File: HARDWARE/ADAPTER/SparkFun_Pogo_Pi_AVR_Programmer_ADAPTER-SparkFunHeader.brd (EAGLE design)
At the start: 15.2 x 31.8 mm, 15 parts, among them J2 CABLE

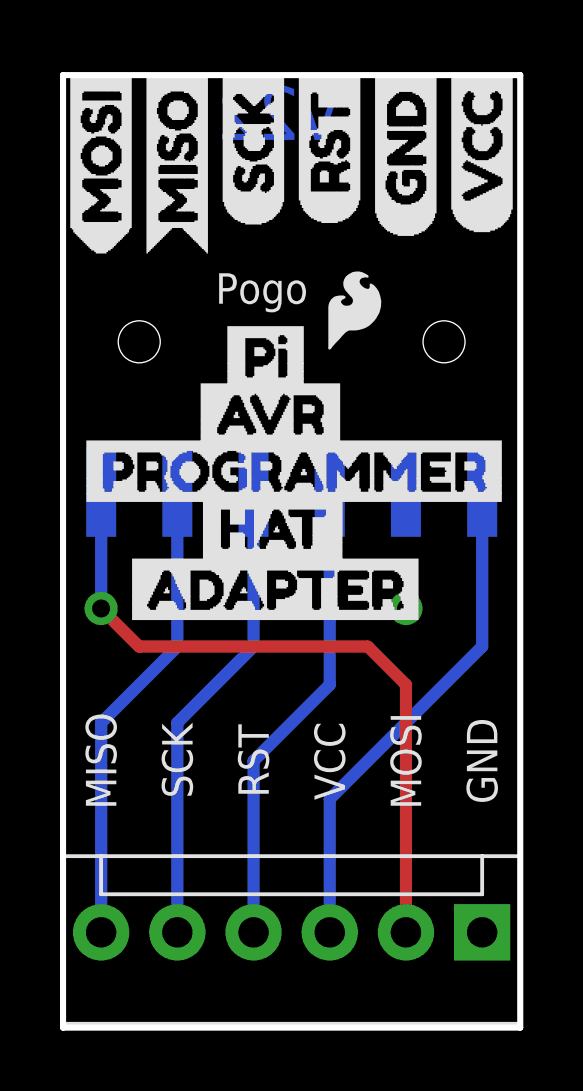
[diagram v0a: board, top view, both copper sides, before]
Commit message: Added proper pogo header.
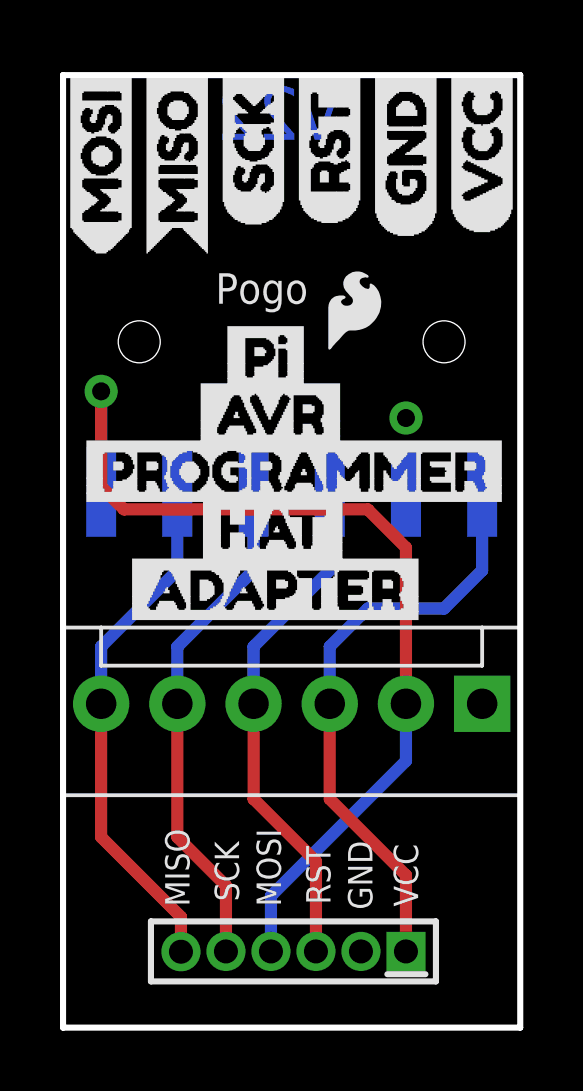
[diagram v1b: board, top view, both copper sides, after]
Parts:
- added U$12: AVR_MINI_PROGSMD, SparkFun-Connectors:AVR_MINI_PROG
- moved JP1 7.62 mm to (14.0, 10.8)
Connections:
- net GND_C: now also U$12.2
- net MISO_C: now also U$12.6
- net MOSI_C: now also U$12.4
- net RST_C: now also U$12.3
- net SCK_C: now also U$12.5
- net VCC_C: now also U$12.1
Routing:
- net MOSI_C: track 23.4 -> 32.9 mm
- net VCC_C: track 16.8 -> 20.0 mm
- net MISO_C: track 15.7 -> 17.5 mm
- net RST_C: track 15.7 -> 17.2 mm
- net SCK_C: track 15.7 -> 17.0 mm
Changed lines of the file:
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@@
 <text x="-10.16" y="-15.24" size="1.778" layer="19" font="vector">Modified by: Michael Moskie</text>
 <text x="5.08" y="24.13" size="1.016" layer="21" font="vector">Pogo</text>
-<text x="1.27" y="8.89" size="1.016" layer="21" font="vector" rot="R90" align="center">MISO</text>
-<text x="3.81" y="8.89" size="1.016" layer="21" font="vector" rot="R90" align="center">SCK</text>
-<text x="6.35" y="8.89" size="1.016" layer="21" font="vector" rot="R90" align="center">RST</text>
-<text x="8.89" y="8.89" size="1.016" layer="21" font="vector" rot="R90" align="center">VCC</text>
-<text x="11.43" y="8.89" size="1.016" layer="21" font="vector" rot="R90" align="center">MOSI</text>
-<text x="13.97" y="8.89" size="1.016" layer="21" font="vector" rot="R90" align="center">GND</text>
+<text x="11.43" y="5.08" size="0.8128" layer="21" font="vector" rot="R270" align="center">VCC</text>
+<text x="9.906" y="5.08" size="0.8128" layer="21" font="vector" rot="R270" align="center">GND</text>
+<text x="8.509" y="5.08" size="0.8128" layer="21" font="vector" rot="R270" align="center">RST</text>
+<text x="6.858" y="5.334" size="0.8128" layer="21" font="vector" rot="R270" align="center">MOSI</text>
+<text x="5.461" y="5.207" size="0.8128" layer="21" font="vector" rot="R270" align="center">SCK</text>
+<text x="3.81" y="5.334" size="0.8128" layer="21" font="vector" rot="R90" align="center">MISO</text>
 </plain>
 <attributes>
@@
 <element name="U$10" library="buzzard_labels (11)" package="HAT3" value="" x="4.064" y="16.637"/>
 <element name="U$11" library="buzzard_labels (11)" package="ADAPTER4" value="" x="1.651" y="14.605"/>
-<element name="JP1" library="SparkFun-Connectors" package="MOLEX-1X6" value="" x="13.97" y="3.175" rot="R180"/>
+<element name="JP1" library="SparkFun-Connectors" package="MOLEX-1X6" value="" x="13.97" y="10.795" rot="R180"/>
+<element name="U$12" library="SparkFun-Connectors" package="AVR_MINI_PROG" value="AVR_MINI_PROGSMD" x="11.43" y="2.54" rot="R180"/>
 </elements>
 <signals>
@@
 <contactref element="J2" pad="1"/>
 <contactref element="JP1" pad="2"/>
-<wire x1="11.43" y1="3.175" x2="11.43" y2="11.43" width="0.4064" layer="1"/>
-<wire x1="11.43" y1="11.43" x2="10.16" y2="12.7" width="0.4064" layer="1"/>
-<wire x1="10.16" y1="12.7" x2="2.54" y2="12.7" width="0.4064" layer="1"/>
-<wire x1="2.54" y1="12.7" x2="1.27" y2="13.97" width="0.4064" layer="1"/>
-<via x="1.27" y="13.97" extent="1-16" drill="0.6"/>
-<wire x1="1.27" y1="13.97" x2="1.27" y2="17.86" width="0.4064" layer="16"/>
+<contactref element="U$12" pad="4"/>
+<wire x1="6.93" y1="2.54" x2="6.93" y2="4.39" width="0.4064" layer="16"/>
+<wire x1="6.93" y1="4.39" x2="11.43" y2="8.89" width="0.4064" layer="16"/>
+<wire x1="11.43" y1="8.89" x2="11.43" y2="10.795" width="0.4064" layer="16"/>
+<wire x1="1.27" y1="17.86" x2="1.27" y2="21.209" width="0.4064" layer="16"/>
+<via x="1.27" y="21.209" extent="1-16" drill="0.6"/>
+<wire x1="1.27" y1="21.209" x2="1.27" y2="18.034" width="0.4064" layer="1"/>
+<wire x1="1.27" y1="18.034" x2="2.032" y2="17.272" width="0.4064" layer="1"/>
+<wire x1="2.032" y1="17.272" x2="10.16" y2="17.272" width="0.4064" layer="1"/>
+<wire x1="10.16" y1="17.272" x2="11.43" y2="16.002" width="0.4064" layer="1"/>
+<wire x1="11.43" y1="10.795" x2="11.43" y2="16.002" width="0.4064" layer="1"/>
 </signal>
 <signal name="MISO_C">
 <contactref element="J2" pad="2"/>
 <contactref element="JP1" pad="6"/>
-<wire x1="1.27" y1="3.175" x2="1.27" y2="10.16" width="0.4064" layer="16"/>
-<wire x1="3.81" y1="17.86" x2="3.81" y2="12.7" width="0.4064" layer="16"/>
-<wire x1="3.81" y1="12.7" x2="1.27" y2="10.16" width="0.4064" layer="16"/>
+<contactref element="U$12" pad="6"/>
+<wire x1="3.93" y1="2.53" x2="3.93" y2="3.69" width="0.4064" layer="1"/>
+<wire x1="3.93" y1="3.69" x2="1.27" y2="6.35" width="0.4064" layer="1"/>
+<wire x1="1.27" y1="6.35" x2="1.27" y2="10.795" width="0.4064" layer="1"/>
+<wire x1="3.81" y1="17.86" x2="3.81" y2="15.24" width="0.4064" layer="16"/>
+<wire x1="1.27" y1="10.795" x2="1.27" y2="12.7" width="0.4064" layer="16"/>
+<wire x1="1.27" y1="12.7" x2="3.81" y2="15.24" width="0.4064" layer="16"/>
 </signal>
 <signal name="SCK_C">
 <contactref element="J2" pad="3"/>
 <contactref element="JP1" pad="5"/>
-<wire x1="3.81" y1="3.175" x2="3.81" y2="10.16" width="0.4064" layer="16"/>
-<wire x1="6.35" y1="17.86" x2="6.35" y2="12.7" width="0.4064" layer="16"/>
-<wire x1="6.35" y1="12.7" x2="3.81" y2="10.16" width="0.4064" layer="16"/>
+<contactref element="U$12" pad="5"/>
+<wire x1="5.43" y1="2.54" x2="5.43" y2="4.73" width="0.4064" layer="1"/>
+<wire x1="5.43" y1="4.73" x2="3.81" y2="6.35" width="0.4064" layer="1"/>
+<wire x1="3.81" y1="6.35" x2="3.81" y2="10.795" width="0.4064" layer="1"/>
+<wire x1="6.35" y1="17.86" x2="6.35" y2="15.24" width="0.4064" layer="16"/>
+<wire x1="6.35" y1="15.24" x2="3.81" y2="12.7" width="0.4064" layer="16"/>
+<wire x1="3.81" y1="12.7" x2="3.81" y2="10.795" width="0.4064" layer="16"/>
 </signal>
 <signal name="RST_C">
 <contactref element="J2" pad="4"/>
 <contactref element="JP1" pad="4"/>
-<wire x1="8.89" y1="17.86" x2="8.89" y2="11.43" width="0.4064" layer="16"/>
-<wire x1="8.89" y1="11.43" x2="6.35" y2="8.89" width="0.4064" layer="16"/>
-<wire x1="6.35" y1="8.89" x2="6.35" y2="3.175" width="0.4064" layer="16"/>
+<contactref element="U$12" pad="3"/>
+<wire x1="6.35" y1="10.795" x2="6.35" y2="7.62" width="0.4064" layer="1"/>
+<wire x1="6.35" y1="7.62" x2="8.43" y2="5.54" width="0.4064" layer="1"/>
+<wire x1="8.43" y1="2.54" x2="8.43" y2="5.54" width="0.4064" layer="1"/>
+<wire x1="8.89" y1="17.86" x2="8.89" y2="15.24" width="0.4064" layer="16"/>
+<wire x1="8.89" y1="15.24" x2="6.35" y2="12.7" width="0.4064" layer="16"/>
+<wire x1="6.35" y1="12.7" x2="6.35" y2="10.795" width="0.4064" layer="16"/>
 </signal>
 <signal name="GND_C">
@@
 </polygon>
 <contactref element="JP1" pad="1"/>
-<via x="11.43" y="13.97" extent="1-16" drill="0.6"/>
+<contactref element="U$12" pad="2"/>
+<via x="11.43" y="20.32" extent="1-16" drill="0.6"/>
 </signal>
 <signal name="VCC_C">
 <contactref element="J2" pad="6"/>
 <contactref element="JP1" pad="3"/>
-<wire x1="13.97" y1="17.86" x2="13.97" y2="12.7" width="0.4064" layer="16"/>
-<wire x1="13.97" y1="12.7" x2="8.89" y2="7.62" width="0.4064" layer="16"/>
-<wire x1="8.89" y1="3.175" x2="8.89" y2="7.62" width="0.4064" layer="16"/>
+<contactref element="U$12" pad="1"/>
+<wire x1="11.43" y1="2.54" x2="11.43" y2="5.08" width="0.4064" layer="1"/>
+<wire x1="11.43" y1="5.08" x2="8.89" y2="7.62" width="0.4064" layer="1"/>
+<wire x1="8.89" y1="7.62" x2="8.89" y2="10.795" width="0.4064" layer="1"/>
+<wire x1="13.97" y1="17.86" x2="13.97" y2="15.24" width="0.4064" layer="16"/>
+<wire x1="13.97" y1="15.24" x2="12.7" y2="13.97" width="0.4064" layer="16"/>
+<wire x1="12.7" y1="13.97" x2="10.16" y2="13.97" width="0.4064" layer="16"/>
+<wire x1="10.16" y1="13.97" x2="8.89" y2="12.7" width="0.4064" layer="16"/>
+<wire x1="8.89" y1="12.7" x2="8.89" y2="10.795" width="0.4064" layer="16"/>
 </signal>
 </signals>
